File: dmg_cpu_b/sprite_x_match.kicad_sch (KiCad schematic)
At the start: 114 parts

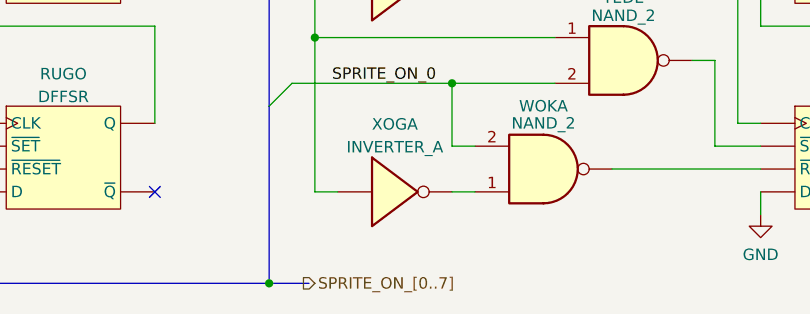
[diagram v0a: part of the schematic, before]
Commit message: bg and sp px shifters added.
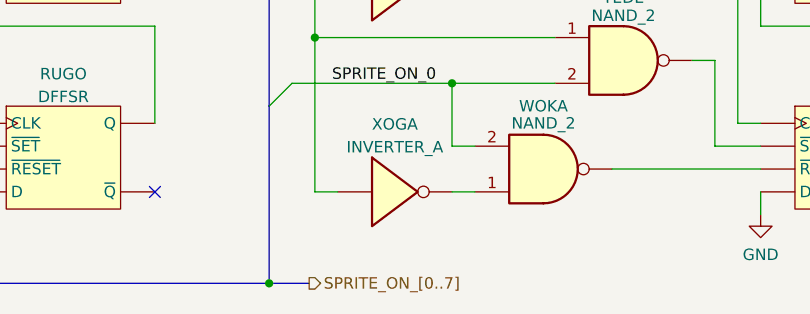
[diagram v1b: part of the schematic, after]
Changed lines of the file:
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@@
     (effects (font (size 1.27 1.27)) (justify left))
   )
-  (hierarchical_label "SPRITE_ON_[0..7]" (shape output) (at 330.2 236.22 0)
+  (hierarchical_label "SPRITE_ON_[0..7]" (shape output) (at 330.835 236.22 0)
     (effects (font (size 1.27 1.27)) (justify left))
   )

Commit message: All sheets captured. Serious tidying is required in PPU section.
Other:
- company: (none) -> CC-BY-SA-4.0 Régis Galland & Michael Singer -- Derived work from Furrtek
- title: (none) -> DMG CPU B
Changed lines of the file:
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@@
 (kicad_sch (version 20211123) (generator eeschema)
   (paper "A3")
+  (title_block
+    (title "DMG CPU B")
+    (date "2022-05-19")
+    (rev "0")
+    (company "CC-BY-SA-4.0 Régis Galland & Michael Singer -- Derived work from Furrtek")
+    (comment 1 "https://github.com/msinger/dmg-schematics")
+  )
   (junction (at 204.47 51.435) (diameter 0) (color 0 0 0 0)
   )

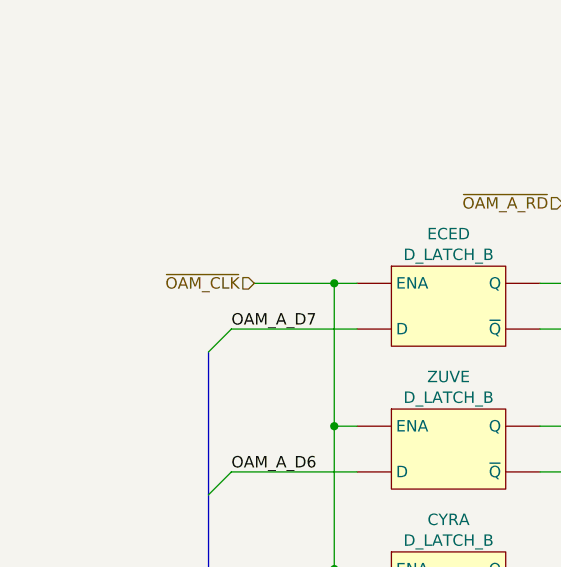
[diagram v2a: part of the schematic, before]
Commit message: Changes made based on review. PPU hierarchcal sheet work started.
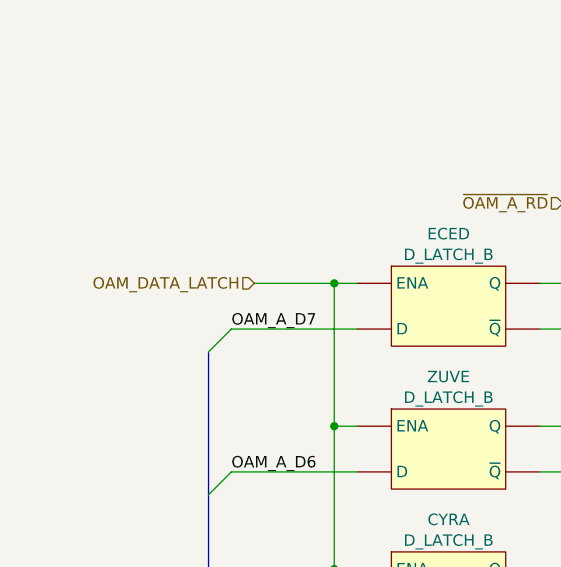
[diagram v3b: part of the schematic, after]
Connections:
- net ~{OAM_CLK} renamed OAM_DATA_LATCH
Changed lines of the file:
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@@
     (effects (font (size 1.27 1.27)) (justify right))
   )
-  (hierarchical_label "~{OAM_CLK}" (shape input) (at 36.83 86.36 180)
+  (hierarchical_label "OAM_DATA_LATCH" (shape input) (at 36.83 86.36 180)
     (effects (font (size 1.27 1.27)) (justify right))
   )

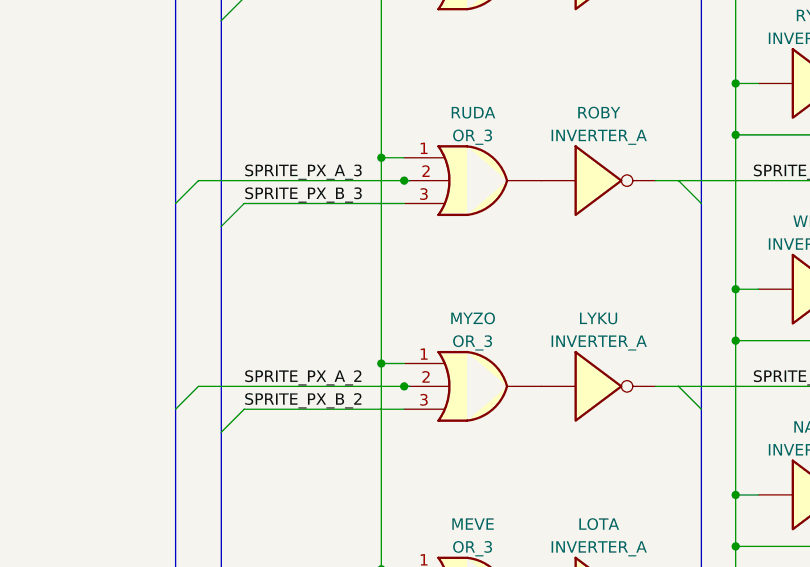
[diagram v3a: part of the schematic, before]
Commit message: All connections between sheet are complete. Can still do with a good tidy up.
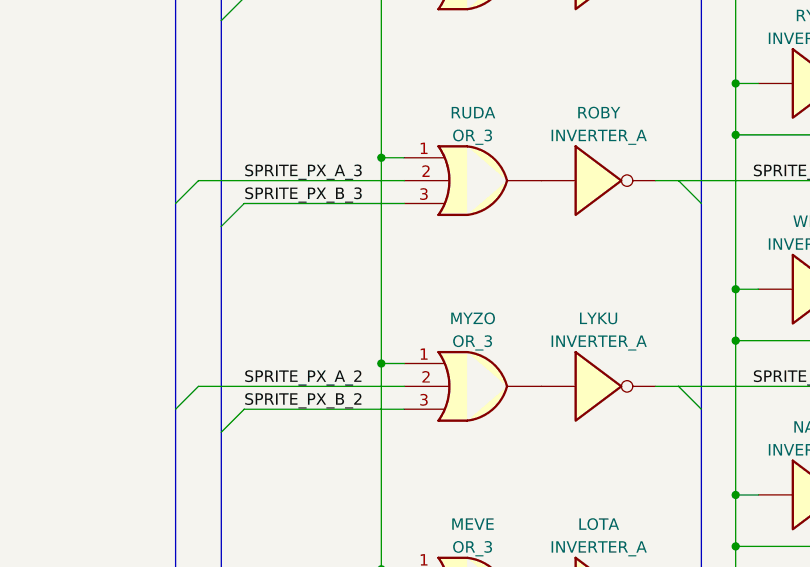
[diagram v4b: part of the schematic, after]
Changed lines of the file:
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@@
   (junction (at 130.81 102.235) (diameter 0) (color 0 0 0 0)
   )
-  (junction (at 207.01 168.275) (diameter 0) (color 0 0 0 0)
-  )
   (junction (at 378.46 104.14) (diameter 0) (color 0 0 0 0)
   )
@@
   (junction (at 204.47 120.015) (diameter 0) (color 0 0 0 0)
   )
-  (junction (at 207.01 145.415) (diameter 0) (color 0 0 0 0)
-  )
   (junction (at 45.72 149.86) (diameter 0) (color 0 0 0 0)
   )
@@
     (stroke (width 0) (type default) (color 0 0 0 0))
   )
-  (wire (pts (xy 207.01 168.275) (xy 207.645 168.275))
-    (stroke (width 0) (type default) (color 0 0 0 0))
-  )
   (wire (pts (xy 334.01 157.48) (xy 331.47 157.48))
     (stroke (width 0) (type default) (color 0 0 0 0))
@@
     (stroke (width 0) (type default) (color 0 0 0 0))
   )
-  (wire (pts (xy 207.01 145.415) (xy 207.645 145.415))
-    (stroke (width 0) (type default) (color 0 0 0 0))
-  )
   (wire (pts (xy 288.29 211.455) (xy 288.29 220.98))
     (stroke (width 0) (type default) (color 0 0 0 0))
@@
   (symbol (lib_id "power:GND") (at 293.37 228.6 0) (unit 1)
     (in_bom yes) (on_board yes) (fields_autoplaced)
-    (property "Reference" "#PWR?" (id 0) (at 293.37 234.95 0)
+    (property "Reference" "#PWR0128" (id 0) (at 293.37 234.95 0)
       (effects (font (size 1.27 1.27)) hide)
     )
@@
   (symbol (lib_id "power:GND") (at 381 228.6 0) (unit 1)
     (in_bom yes) (on_board yes) (fields_autoplaced)
-    (property "Reference" "#PWR?" (id 0) (at 381 234.95 0)
+    (property "Reference" "#PWR0127" (id 0) (at 381 234.95 0)
       (effects (font (size 1.27 1.27)) hide)
     )

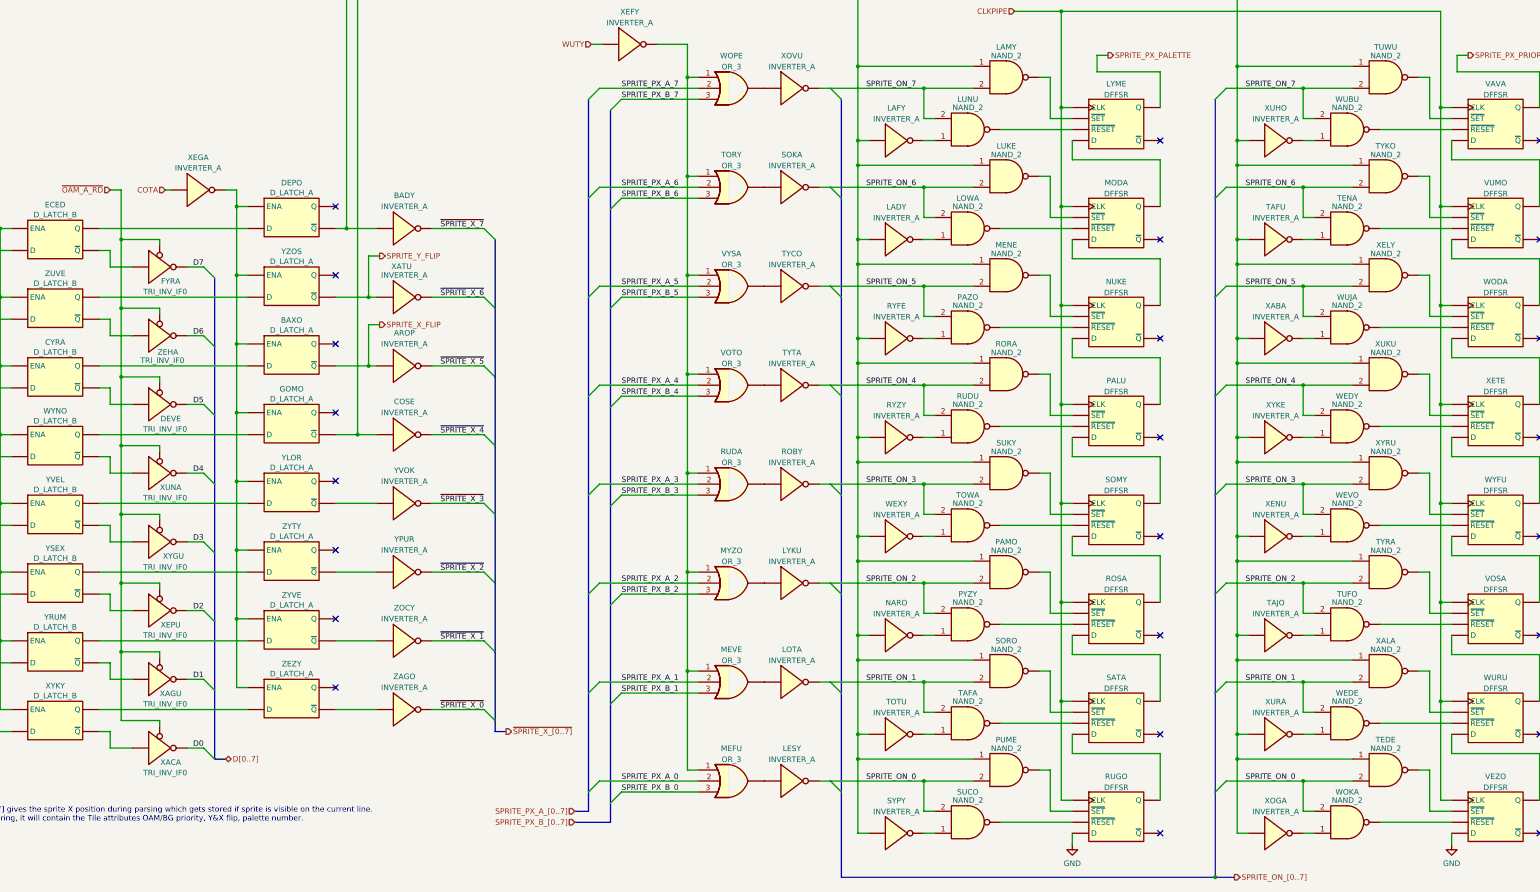
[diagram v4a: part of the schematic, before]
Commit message: Quite a few fixes from review.
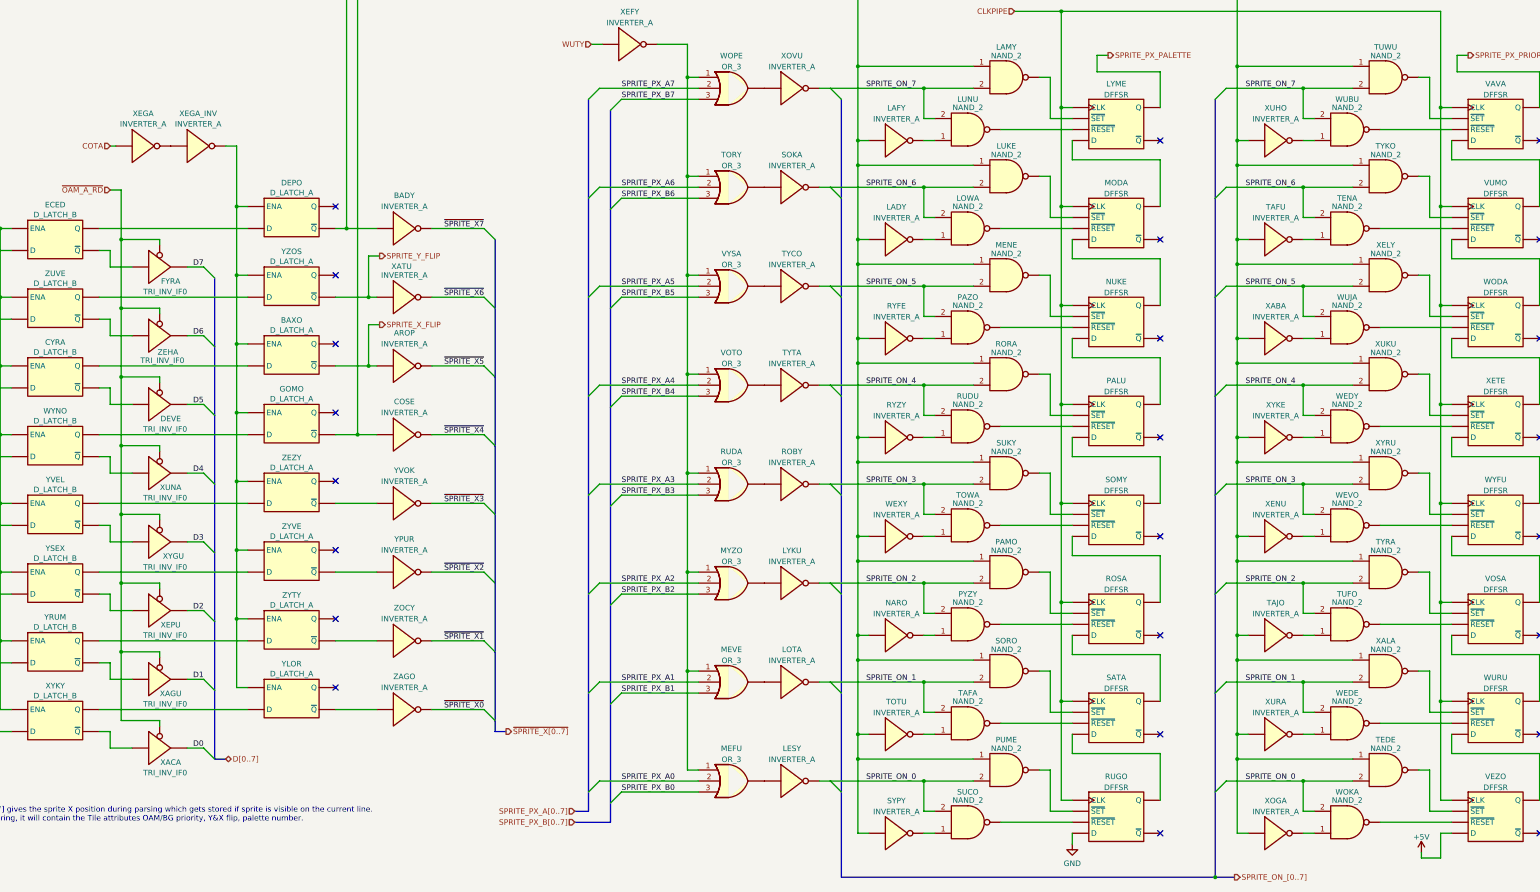
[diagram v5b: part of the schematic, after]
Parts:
- added XEGA_INV: INVERTER_A, symbol DMG_CPU_Cells:INVERTER_A
- DEVE, FYRA, XACA, XAGU, XEPU, XUNA, XYGU, ZEHA: symbol DMG_CPU_Cells:TRI_INV_IF0 -> DMG_CPU_Cells:TRI_BUF_IF0
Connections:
- net D0: now also XACA.4; no longer XACA.3
- net D1: now also XAGU.4; no longer XAGU.3
- net D2: now also XEPU.4; no longer XEPU.3
- net D3: now also XYGU.4; no longer XYGU.3
- net D4: now also XUNA.4; no longer XUNA.3
- net D5: now also DEVE.4; no longer DEVE.3
- net D6: now also ZEHA.4; no longer ZEHA.3
- net D7: now also FYRA.4; no longer FYRA.3
- net GND: no longer VEZO.2 (D)
- net ~{OAM_A_RD}: now also DEVE.2 (~{ENA}), FYRA.2 (~{ENA}), XACA.2 (~{ENA}), XAGU.2 (~{ENA}), XEPU.2 (~{ENA}), XUNA.2 (~{ENA}), XYGU.2 (~{ENA}), ZEHA.2 (~{ENA}); no longer DEVE.1 (~{ENA}), FYRA.1 (~{ENA}), XACA.1 (~{ENA}), XAGU.1 (~{ENA}), XEPU.1 (~{ENA}), XUNA.1 (~{ENA}), XYGU.1 (~{ENA}), ZEHA.1 (~{ENA})
- net at YPUR.1: now also ZYVE.5 (~{Q}); no longer ZYTY.5 (~{Q})
- net at YRUM.4 (~{Q}): now also XAGU.1 (IN), XAGU.3 (IN); no longer XAGU.2
- net at BAXO.1 (~{ENA}), BAXO.3 (ENA), DEPO.1 (~{ENA})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: now also XEGA_INV.2; no longer XEGA.2
- net at ZYTY.2 (D): now also YRUM.3 (Q); no longer YSEX.3 (Q)
- net at YVOK.1: now also ZEZY.5 (~{Q}); no longer YLOR.5 (~{Q})
- net at ZAGO.1: now also YLOR.5 (~{Q}); no longer ZEZY.5 (~{Q})
- net at ZYVE.2 (D): now also YSEX.3 (Q); no longer YRUM.3 (Q)
- net at ZOCY.1: now also ZYTY.5 (~{Q}); no longer ZYVE.5 (~{Q})
- net at CYRA.4 (~{Q}): now also DEVE.1 (IN), DEVE.3 (IN); no longer DEVE.2
- net at YSEX.4 (~{Q}): now also XEPU.1 (IN), XEPU.3 (IN); no longer XEPU.2
- net at XYKY.4 (~{Q}): now also XACA.1 (IN), XACA.3 (IN); no longer XACA.2
- net at YLOR.2 (D): now also XYKY.3 (Q); no longer YVEL.3 (Q)
- net at ZUVE.4 (~{Q}): now also ZEHA.1 (IN), ZEHA.3 (IN); no longer ZEHA.2
- net at ZEZY.2 (D): now also YVEL.3 (Q); no longer XYKY.3 (Q)
- net at YVEL.4 (~{Q}): now also XYGU.1 (IN), XYGU.3 (IN); no longer XYGU.2
- net at ECED.4 (~{Q}): now also FYRA.1 (IN), FYRA.3 (IN); no longer FYRA.2
- net at WYNO.4 (~{Q}): now also XUNA.1 (IN), XUNA.3 (IN); no longer XUNA.2
- net SPRITE_PX_A_0 renamed SPRITE_PX_A0
- net SPRITE_PX_A_1 renamed SPRITE_PX_A1
- net SPRITE_PX_A_2 renamed SPRITE_PX_A2
- net SPRITE_PX_A_3 renamed SPRITE_PX_A3
- net SPRITE_PX_A_4 renamed SPRITE_PX_A4
- net SPRITE_PX_A_5 renamed SPRITE_PX_A5
- net SPRITE_PX_A_6 renamed SPRITE_PX_A6
- net SPRITE_PX_A_7 renamed SPRITE_PX_A7
- net SPRITE_PX_B_0 renamed SPRITE_PX_B0
- net SPRITE_PX_B_1 renamed SPRITE_PX_B1
- net SPRITE_PX_B_2 renamed SPRITE_PX_B2
- net SPRITE_PX_B_3 renamed SPRITE_PX_B3
- net SPRITE_PX_B_4 renamed SPRITE_PX_B4
- net SPRITE_PX_B_5 renamed SPRITE_PX_B5
- net SPRITE_PX_B_6 renamed SPRITE_PX_B6
- net SPRITE_PX_B_7 renamed SPRITE_PX_B7
- net ~{SPRITE_X_0} renamed ~{SPRITE_X0}
- net ~{SPRITE_X_1} renamed ~{SPRITE_X1}
- net ~{SPRITE_X_2} renamed ~{SPRITE_X2}
- net ~{SPRITE_X_3} renamed ~{SPRITE_X3}
- net ~{SPRITE_X_4} renamed ~{SPRITE_X4}
- net ~{SPRITE_X_5} renamed ~{SPRITE_X5}
- net ~{SPRITE_X_6} renamed ~{SPRITE_X6}
- net ~{SPRITE_X_7} renamed ~{SPRITE_X7}
- new net: XEGA.2, XEGA_INV.1
- new net +5V: VEZO.2 (D)
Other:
- moved on the sheet: XEGA, YLOR, ZEZY, ZYTY, ZYVE
